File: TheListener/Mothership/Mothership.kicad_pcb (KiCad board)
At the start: 2 copper layers, 65 parts, among them J1 RJ45, J2 RJ45, J3 RJ45, J4 RJ45, J5 RJ45, J6 RJ45, J7 RJ45, J8 RJ45, J9 Conn_01x02_Female, U1 SP3491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

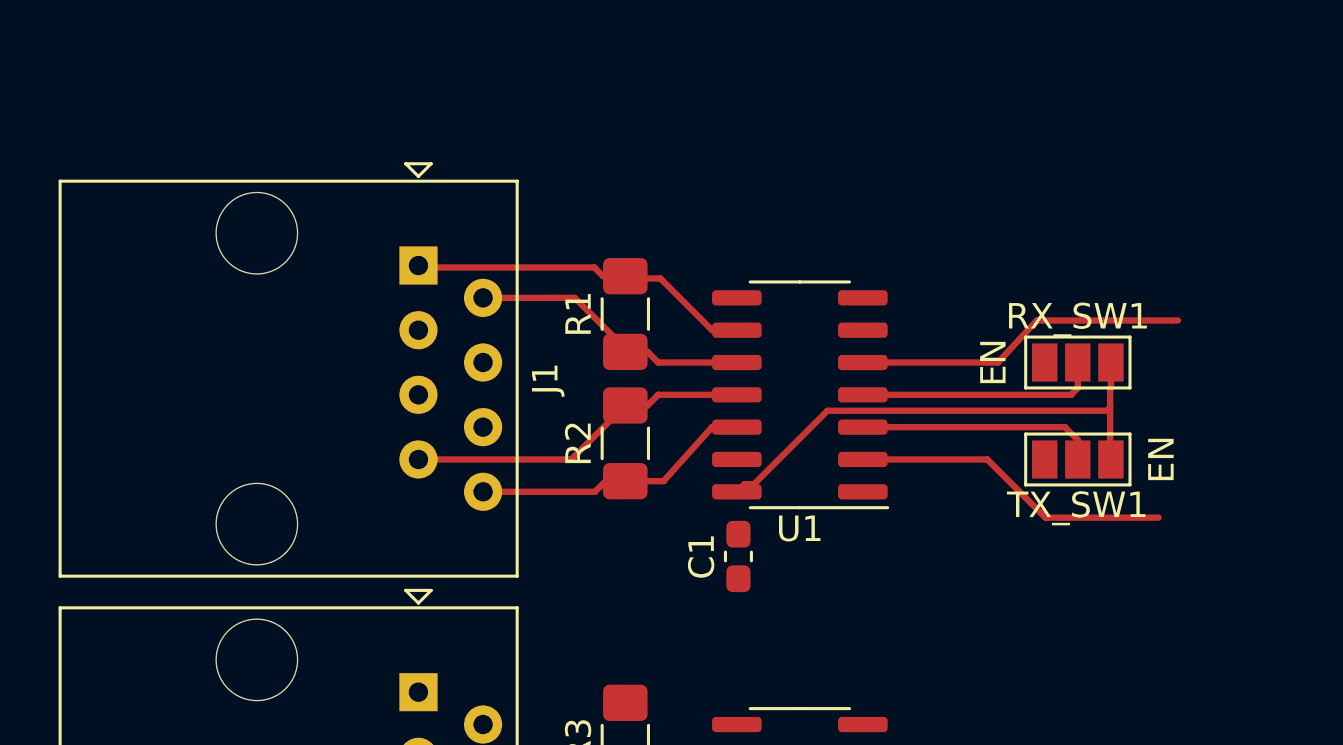
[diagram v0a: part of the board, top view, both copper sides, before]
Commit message: layout for one port
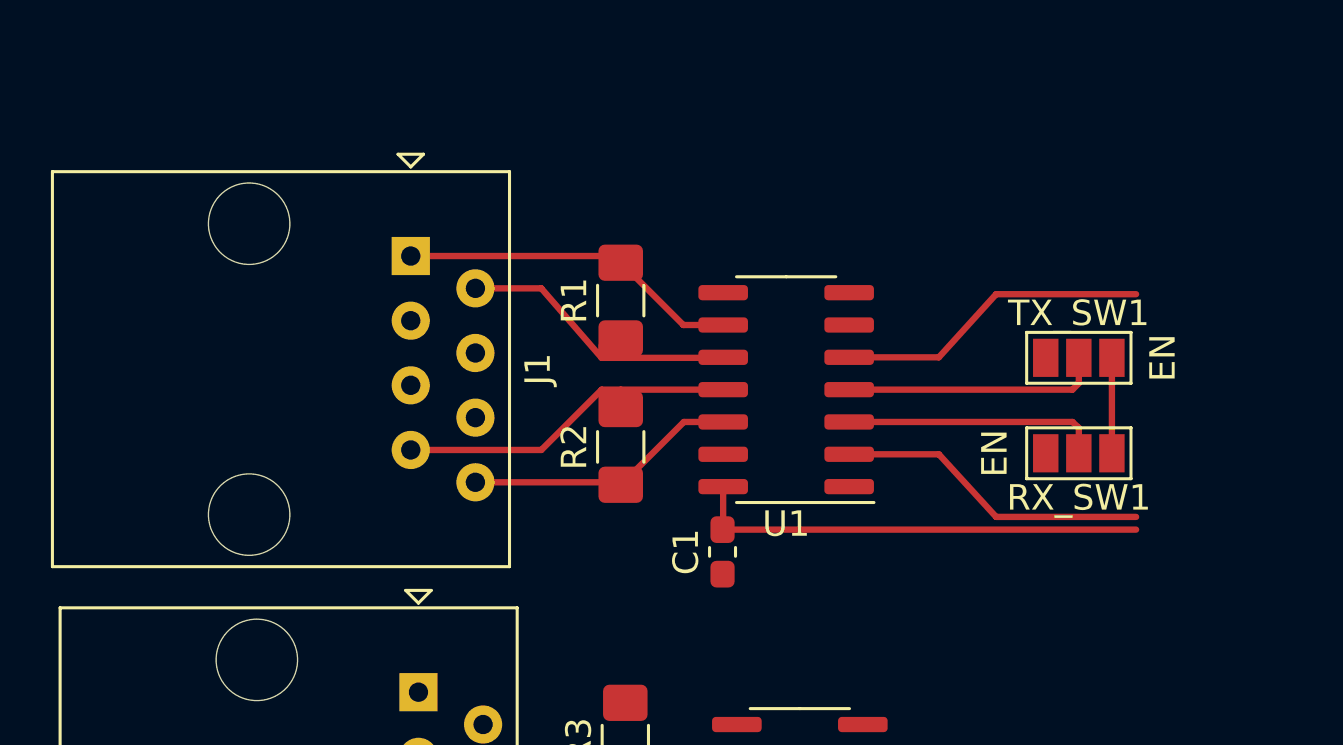
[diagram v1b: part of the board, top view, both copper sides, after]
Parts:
- moved TX_SW1 3.99 mm to (61.0, 43.2)
- moved RX_SW1 3.57 mm to (61.0, 47.0)
- moved C1 0.65 mm to (47.0, 50.9)
- moved U1 0.58 mm to (49.5, 44.5)
- moved R1 0.56 mm to (43.0, 41.0)
- moved J1 0.48 mm to (34.8, 39.2)
- moved R2 0.23 mm to (43.0, 46.8)
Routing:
- net VCC1: track 19.9 -> 21.7 mm
- net Net-(J1-Pad2): track 11.3 -> 12.3 mm
- net T_1: track 13.1 -> 12.4 mm
- net Net-(RX_SW1-Pad2): track 9.42 -> 10.1 mm
- net Net-(TX_SW1-Pad2): track 9.56 -> 10.1 mm
- net Net-(J1-Pad1): track 13.6 -> 13.0 mm

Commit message: updates to layout
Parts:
- moved RX_SW1 2.75 mm to (58.2, 47.0)
- moved TX_SW1 2.75 mm to (58.2, 43.2)
- moved C1 0.50 mm to (47.5, 50.9)
- moved U1 0.50 mm to (50.0, 44.5)
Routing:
- net T_1: track 12.4 -> 2.27 mm
- net R_1: track 12.4 -> 2.27 mm
- net GND: track 0.00 -> 9.05 mm, vias 0 -> 7
- net Net-(J1-Pad8): track 10.3 -> 15.6 mm
- net Net-(TX_SW1-Pad2): track 10.1 -> 6.88 mm
- net Net-(J1-Pad2): track 12.3 -> 15.5 mm
- net Net-(RX_SW1-Pad2): track 10.1 -> 7.21 mm
- net Net-(J1-Pad1): track 13.0 -> 15.6 mm
- net Net-(J1-Pad7): track 14.0 -> 15.4 mm
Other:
- net class Default: clearance 0.2 -> 0.25
- net class High Current added: clearance 0.5, trace_width 5, via_dia 1.6, via_drill 0.8
- net class Low Current added: clearance 0.25, trace_width 1, via_dia 0.8, via_drill 0.4
- rule pad_to_mask_clearance: 0.051 -> 0.05
- rule trace_clearance: 0.2 -> 0.25
- rule via_min_size: 0.4 -> 0.6

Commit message: almost
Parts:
- moved U12 126.8 mm to (208.5, 66.2)
- moved U10 120.1 mm to (28.5, 134.5)
- moved C10 109.7 mm to (30.1, 128.2)
- moved J9 90.9 mm to (103.9, 99.3), turned to 180 degrees
- moved C11 75.4 mm to (102.1, 89.6), turned to 0 degrees
- moved U9 72.1 mm to (37.7, 24.9), turned to 180 degrees
- moved C8 71.0 mm to (104.2, 125.6)
- moved C9 68.9 mm to (44.0, 26.5), turned to 270 degrees
- moved R16 67.6 mm to (101.2, 129.2), turned to 180 degrees
- moved RX_SW8 64.6 mm to (101.2, 114.0), turned to 90 degrees
- moved U8 62.9 mm to (98.8, 122.2), turned to 270 degrees
- moved J8 61.8 mm to (93.8, 137.5), turned to 0 degrees
- moved R15 59.9 mm to (95.2, 129.2), turned to 180 degrees
- moved TX_SW8 59.4 mm to (97.5, 114.0), turned to 270 degrees
- moved C7 47.4 mm to (87.2, 125.6)
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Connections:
- C9 pad 1: VCC1 -> (no net)
- C9 pad 2: GND -> (no net)
- U9 pad 1: GND -> (no net)
- U9 pad 2: VCC1 -> (no net)
- U9 pad 3: +5V -> (no net)
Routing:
- net VCC2: track 0.00 -> 213.0 mm, vias 0 -> 33
- net VCC1: track 21.7 -> 171.7 mm, vias 0 -> 8
- net GND: track 9.05 -> 88.8 mm, vias 7 -> 87
- net (no net): track 0.00 -> 48.9 mm, vias 0 -> 31
- net +24V: track 0.00 -> 28.6 mm
- net Net-(J8-Pad7): track 0.00 -> 13.8 mm
- net Net-(J7-Pad7): track 0.00 -> 13.8 mm
- net Net-(J6-Pad7): track 0.00 -> 13.8 mm
- net Net-(J5-Pad7): track 0.00 -> 13.8 mm
- net Net-(J4-Pad7): track 0.00 -> 13.8 mm
- net Net-(J3-Pad7): track 0.00 -> 13.8 mm
- net Net-(J2-Pad7): track 0.00 -> 13.8 mm
- net Net-(J6-Pad1): track 0.00 -> 13.8 mm
- net Net-(J5-Pad1): track 0.00 -> 13.8 mm
- net Net-(J8-Pad1): track 0.00 -> 13.8 mm
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- added copper zone on B.Cu, net (none)
- added copper zone on F.Cu, net (none)
- added copper zone on F.Cu, net +5V
- added copper zone on B.Cu, net VCC2
- added copper zone on F.Cu, net VCC2
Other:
- rule via_min_size: 0.6 -> 0.8

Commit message: .
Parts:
- moved U12 107.8 mm to (103.8, 40.8)
- moved U9 26.6 mm to (64.2, 27.2), turned to 90 degrees
- moved U10 23.1 mm to (37.5, 113.2), turned to 180 degrees
- moved C9 19.9 mm to (62.6, 33.5), turned to 180 degrees
- moved C10 19.1 mm to (43.8, 114.9), turned to 270 degrees
- moved J9 13.4 mm to (108.8, 86.8), turned to 270 degrees
- moved C5 8.55 mm to (60.0, 130.9)
- moved C6 8.55 mm to (77.0, 130.9)
- moved C7 8.55 mm to (94.0, 130.9)
- moved C8 8.55 mm to (111.0, 130.9)
- moved J5 8.55 mm to (49.5, 142.8)
- moved J6 8.55 mm to (66.5, 142.8)
- moved J7 8.55 mm to (83.5, 142.8)
- moved J8 8.55 mm to (100.5, 142.8)
- moved R10 8.55 mm to (56.9, 134.5)
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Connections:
- C9 pad 1: (no net) -> VCC1
- C9 pad 2: (no net) -> GND
- U9 pad 1: (no net) -> GND
- U9 pad 2: (no net) -> VCC1
- U9 pad 3: (no net) -> +5V
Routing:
- net +5V: track 4.00 -> 113.7 mm
- net GND: track 88.8 -> 142.7 mm, vias 87 -> 81
- net (no net): track 48.9 -> 0.00 mm, vias 31 -> 0
- net +24V: track 28.6 -> 53.6 mm
- net VCC2: track 213.0 -> 191.4 mm
- net VCC1: track 171.7 -> 191.5 mm, vias 8 -> 33
- added copper zone on F.Cu, net VCC1
- removed copper zone on F.Cu, net (none)

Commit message: all except signals; needs refinement of power
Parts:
- moved U12 86.5 mm to (26.2, 79.2), turned to 270 degrees
- moved U10 86.0 mm to (123.5, 114.5), turned to 270 degrees
- moved J1 74.8 mm to (109.5, 36.0), turned to 180 degrees
- moved C10 73.2 mm to (111.2, 86.4), turned to 90 degrees
- moved J9 65.2 mm to (44.7, 74.8)
- moved R1 65.1 mm to (108.0, 44.2), turned to 0 degrees
- moved J2 61.2 mm to (92.5, 36.0), turned to 180 degrees
- moved U9 60.2 mm to (123.3, 38.9)
- moved J4 59.2 mm to (58.5, 36.0), turned to 180 degrees
- moved R2 59.1 mm to (102.1, 44.2), turned to 0 degrees
- moved C9 59.1 mm to (111.2, 67.1), turned to 270 degrees
- moved J3 55.2 mm to (75.5, 36.0), turned to 180 degrees
- moved U1 54.9 mm to (104.5, 51.2), turned to 90 degrees
- moved R8 54.0 mm to (51.1, 44.2), turned to 0 degrees
- moved C4 52.9 mm to (48.0, 47.9), turned to 270 degrees
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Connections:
- J9 pad 1: GND -> +24V
- J9 pad 2: +24V -> GND
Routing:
- net +5V: track 113.7 -> 171.9 mm
- net VCC1: track 191.5 -> 221.9 mm
- net GND: track 142.7 -> 113.9 mm, vias 81 -> 69
- net +24V: track 53.6 -> 31.1 mm
- net VCC2: track 191.4 -> 204.0 mm
- removed copper zone on F.Cu, net +5V

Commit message: wip
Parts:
- moved C11 172.3 mm to (226.6, 74.3)
- moved C12 172.3 mm to (288.2, 73.8)
- moved J9 172.3 mm to (216.9, 72.5)
- moved U11 172.3 mm to (284.8, 72.3)
- moved U12 172.3 mm to (198.5, 77.0)
- moved C10 19.7 mm to (118.9, 104.5), turned to 0 degrees
- moved C9 19.6 mm to (118.6, 49.0), turned to 0 degrees
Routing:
- net +5V: track 171.9 -> 96.8 mm
- net VCC2: track 204.0 -> 209.8 mm, vias 33 -> 34
- net VCC1: track 221.9 -> 226.0 mm
- net T_8: track 10.8 -> 14.3 mm, vias 0 -> 2
- net T_7: track 10.8 -> 14.3 mm, vias 0 -> 2
- net T_6: track 10.8 -> 14.3 mm, vias 0 -> 2
- net T_5: track 10.8 -> 14.3 mm
- net T_4: track 10.8 -> 14.3 mm, vias 0 -> 2
- net T_3: track 10.8 -> 14.3 mm, vias 0 -> 2
- net T_2: track 10.8 -> 14.3 mm, vias 0 -> 2
- net T_1: track 10.8 -> 14.3 mm, vias 0 -> 2
- net R_8: track 10.8 -> 14.3 mm, vias 0 -> 2
- net R_7: track 10.8 -> 14.3 mm, vias 0 -> 2
- net R_5: track 10.8 -> 14.3 mm
- net R_4: track 10.8 -> 14.3 mm, vias 0 -> 2
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- added copper zone on B.Cu, net VCC1
- removed copper zone on B.Cu, net (none)

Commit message: wip
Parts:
- moved C12 157.3 mm to (131.6, 59.4), turned to 90 degrees
- moved U11 147.9 mm to (137.6, 58.7), turned to 0 degrees
- moved U12 121.8 mm to (76.7, 79.2), turned to 180 degrees
- moved C11 96.9 mm to (139.6, 116.9), turned to 0 degrees
- moved J9 95.8 mm to (137.8, 126.5), turned to 0 degrees
- moved C9 5.90 mm to (115.1, 53.8), turned to 180 degrees
- moved C5 5.00 mm to (59.8, 110.6)
- moved C6 5.00 mm to (76.8, 110.6)
- moved C7 5.00 mm to (93.8, 110.6)
- moved C8 5.00 mm to (110.8, 110.6)
- moved J5 5.00 mm to (49.2, 122.5)
- moved J6 5.00 mm to (66.2, 122.5)
- moved J7 5.00 mm to (83.2, 122.5)
- moved J8 5.00 mm to (100.2, 122.5)
- moved R10 5.00 mm to (56.7, 114.2)
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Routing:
- net +5V: track 96.8 -> 146.5 mm
- net R_1: track 14.3 -> 35.3 mm
- net T_3: track 14.3 -> 32.9 mm
- net R_6: track 10.8 -> 28.7 mm
- net R_8: track 14.3 -> 26.7 mm
- net R_3: track 14.3 -> 26.5 mm
- net R_2: track 14.3 -> 21.2 mm
- net R_4: track 14.3 -> 20.9 mm
- net T_7: track 14.3 -> 16.4 mm
- net T_2: track 14.3 -> 16.3 mm
- net T_6: track 14.3 -> 16.3 mm
- net R_7: track 14.3 -> 16.1 mm
- net R_5: track 14.3 -> 16.1 mm
- net T_1: track 14.3 -> 16.1 mm
- net T_4: track 14.3 -> 16.1 mm
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
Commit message: wip
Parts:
- added R17: 220, Resistor_SMD:R_0603_1608Metric_Pad1.05x0.95mm_HandSolder, F.Cu at (103.0, 74.2)
- added R18: 220, Resistor_SMD:R_0603_1608Metric_Pad1.05x0.95mm_HandSolder, F.Cu at (100.8, 74.0)
- added R19: 220, Resistor_SMD:R_0603_1608Metric_Pad1.05x0.95mm_HandSolder, F.Cu at (98.2, 68.5)
- added R20: 220, Resistor_SMD:R_0603_1608Metric_Pad1.05x0.95mm_HandSolder, F.Cu at (96.0, 74.5)
- added R21: 220, Resistor_SMD:R_0603_1608Metric_Pad1.05x0.95mm_HandSolder, F.Cu at (93.2, 74.2)
- added R22: 220, Resistor_SMD:R_0603_1608Metric_Pad1.05x0.95mm_HandSolder, F.Cu at (90.8, 69.0)
- added R23: 220, Resistor_SMD:R_0603_1608Metric_Pad1.05x0.95mm_HandSolder, F.Cu at (88.0, 68.2)
- added R24: 220, Resistor_SMD:R_0603_1608Metric_Pad1.05x0.95mm_HandSolder, F.Cu at (85.5, 74.2)
- added R25: 220, Resistor_SMD:R_0603_1608Metric_Pad1.05x0.95mm_HandSolder, F.Cu at (83.0, 68.8)
- added R26: 220, Resistor_SMD:R_0603_1608Metric_Pad1.05x0.95mm_HandSolder, F.Cu at (78.0, 67.8)
- added R27: 220, Resistor_SMD:R_0603_1608Metric_Pad1.05x0.95mm_HandSolder, F.Cu at (73.0, 74.2)
- added R28: 220, Resistor_SMD:R_0603_1608Metric_Pad1.05x0.95mm_HandSolder, F.Cu at (75.5, 90.0)
- added R29: 220, Resistor_SMD:R_0603_1608Metric_Pad1.05x0.95mm_HandSolder, F.Cu at (80.5, 90.2)
- added R30: 220, Resistor_SMD:R_0603_1608Metric_Pad1.05x0.95mm_HandSolder, F.Cu at (83.0, 83.8)
- added R31: 220, Resistor_SMD:R_0603_1608Metric_Pad1.05x0.95mm_HandSolder, F.Cu at (93.2, 90.5)
- added R32: 220, Resistor_SMD:R_0603_1608Metric_Pad1.05x0.95mm_HandSolder, F.Cu at (90.8, 90.2)
- U12: footprint Teensy:Teensy35_36 -> TheListener:Teensy35_36_NoMiddlePins
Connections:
- U12 pad 10: T_4 -> Net-(R25-Pad1)
- U12 pad 12: R_5 -> Net-(R26-Pad1)
- U12 pad 14: R_6 -> Net-(R27-Pad1)
- U12 pad 2: R_1 -> Net-(R17-Pad1)
- U12 pad 3: R_2 -> Net-(R18-Pad1)
- U12 pad 4: T_1 -> Net-(R19-Pad1)
- U12 pad 41: T_2 -> Net-(R28-Pad1)
- U12 pad 43: R_7 -> Net-(R29-Pad1)
- U12 pad 44: R_8 -> Net-(R30-Pad1)
- U12 pad 47: T_6 -> Net-(R32-Pad2)
- U12 pad 48: T_7 -> Net-(R31-Pad2)
- U12 pad 5: R_3 -> Net-(R20-Pad1)
- U12 pad 6: R_4 -> Net-(R21-Pad1)
- U12 pad 7: T_8 -> Net-(R22-Pad1)
- U12 pad 8: T_5 -> Net-(R23-Pad1)
- U12 pad 9: T_3 -> Net-(R24-Pad1)
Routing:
- net R_1: track 35.3 -> 14.3 mm
- net Net-(R17-Pad1): track 0.00 -> 21.0 mm
- net Net-(R24-Pad1): track 0.00 -> 19.4 mm
- net Net-(R27-Pad1): track 0.00 -> 18.8 mm
- net T_3: track 32.9 -> 14.3 mm
- net R_6: track 28.7 -> 10.8 mm
- net R_8: track 26.7 -> 14.3 mm
- net Net-(R30-Pad1): track 0.00 -> 12.4 mm
- net R_3: track 26.5 -> 14.3 mm
- net Net-(R20-Pad1): track 0.00 -> 12.2 mm
- net Net-(R18-Pad1): track 0.00 -> 6.95 mm
- net R_2: track 21.2 -> 14.3 mm
- net R_4: track 20.9 -> 14.3 mm
- net Net-(R21-Pad1): track 0.00 -> 6.69 mm
- net T_7: track 16.4 -> 14.3 mm
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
